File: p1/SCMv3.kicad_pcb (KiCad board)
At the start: 2 copper layers, 58.7 x 110.9 mm, 122 parts, among them IC1 40106, IC2 40106, IC3 TL082, J1 ISP, J1-OUT8 JACK-MONO-SWB, J2 Conn_01x02, J2-OUT7 JACK-MONO-SWB, J3 POWER, J3-OUT6 JACK-MONO-SWB, J4-OUT5 JACK-MONO-SWB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

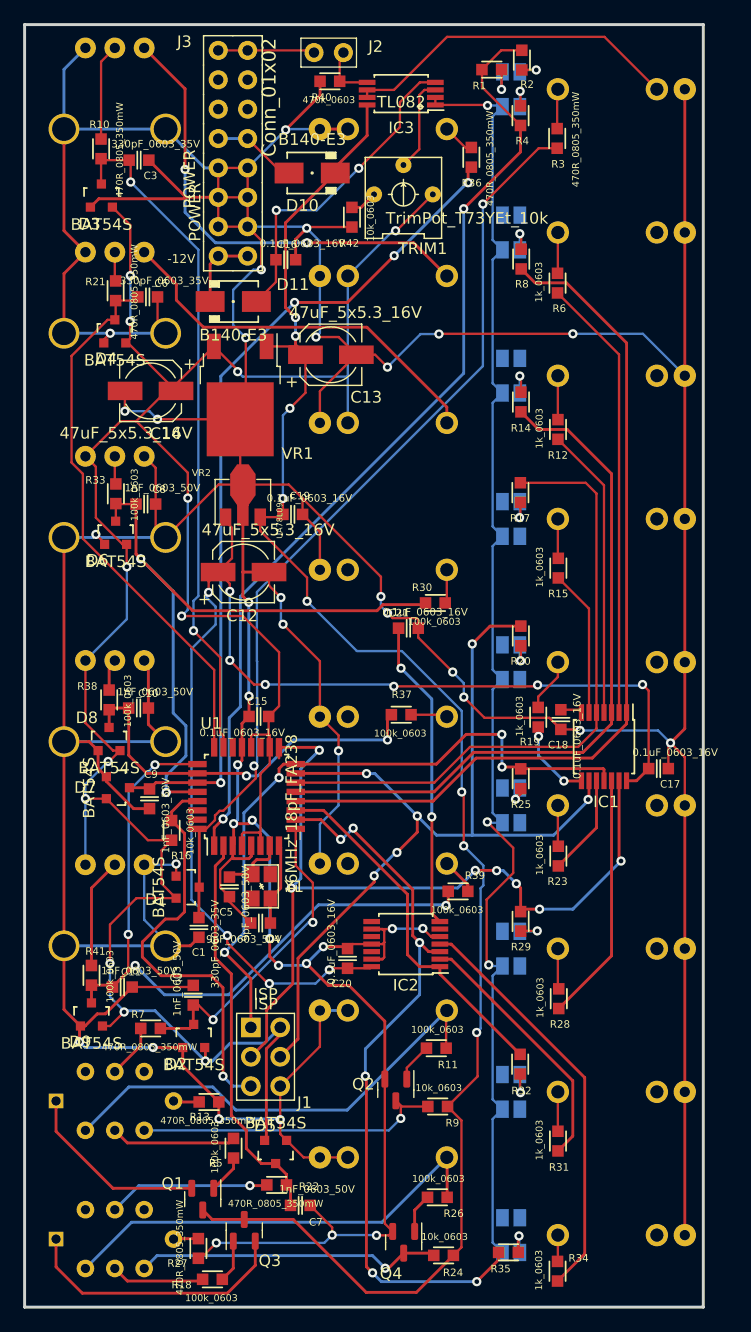
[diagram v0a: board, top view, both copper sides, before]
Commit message: SCM v3 updates
*added missing trace for buttons
*moved trip pot
*flipped pots around
*removed C18 and 21
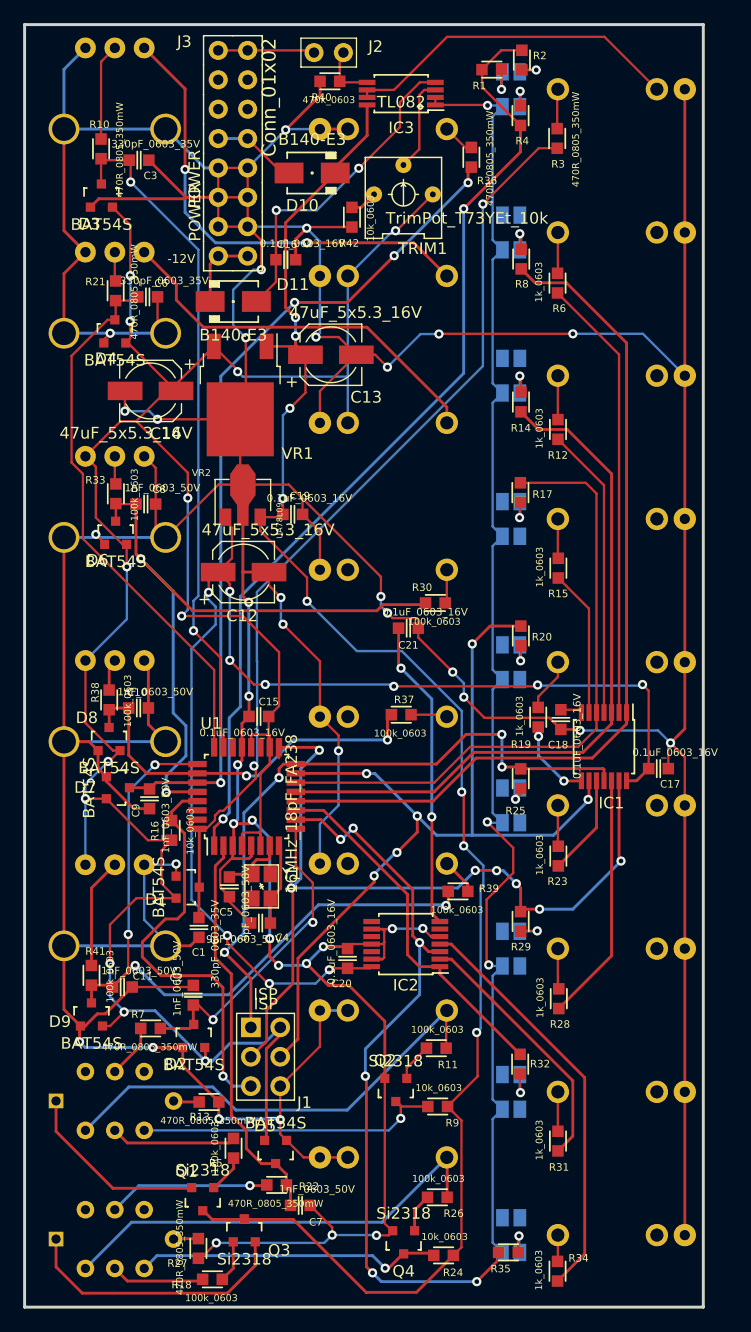
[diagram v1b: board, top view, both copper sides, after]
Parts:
- Q1, Q2, Q3, Q4: footprint Package_TO_SOT_SMD:SOT-23 -> 4ms_Package_SOT:SOT23-3_PO132
- U1: value ATmega328-A -> ATMEGA328-AU
- turned Q1 to 180 degrees
- turned Q2 to 180 degrees
- turned Q3 to 0 degrees
- turned Q4 to 180 degrees
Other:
- rule pad_to_mask_clearance: 0.2 -> 0
